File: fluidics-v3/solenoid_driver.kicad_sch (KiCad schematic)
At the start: 2 parts, among them J5 Screw_Terminal_01x06, U1 TPL7407LDR

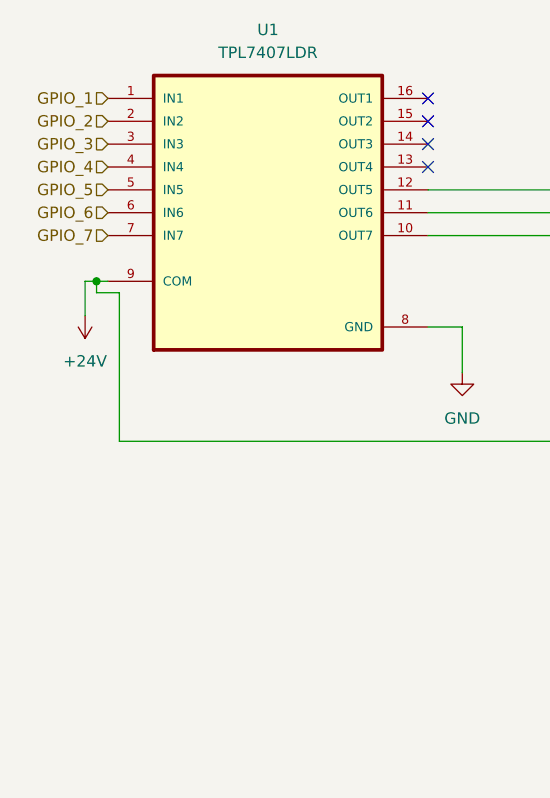
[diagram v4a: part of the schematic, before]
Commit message: v3: +24V soft-start front end, U1 COM bypass, silkscreen and BOM fixes
Power input stage
- Replace TH1 (10 ohm NTC) with a low-side N-channel soft-start: Q1 (F60N80,
  TO-220) with a 100k/68k gate divider (R2/R6) and 0.1u timing cap (C11).
  The NTC sat in series with the whole board and dissipated 1.5-10 W; at
  1.85 A it was already over a 7 mm disc's rating before any valve moved.
- Split ground: /GND1 (J1 shell + pin 2) is now separate from GND, with Q1
  bridging them. Removed a leftover 2.39 mm GND track that still touched
  J1.S2 and shorted straight across Q1.
- Add C12 470u/50V bulk and C13 0.1u HF bypass on +24V. C3 alone left the
  300 kHz - 100 MHz band uncovered while U4 switches at 500 kHz.
- Route the block: gate net kept inside 5 mm of Q1's gate; /GND1 return at
  1.50 mm (4.3 A capacity vs 1.85 A worst case through Q1).

Solenoid driver
- Add C25 0.1u across U1 pin 9 (COM) to GND. That node catches flyback from
  all seven channels and previously reached the +24V plane through ~50 mm of
  0.55 mm trace with nothing local.

Silkscreen
- Raise 403 graphic objects from 0.000/0.100/0.120/0.127 mm to the 0.15 mm
  fab minimum; five were zero-width, which is undefined behaviour. Fix one
  0.45 mm text height and one 0.09 mm stroke.
- Selector valve legend: label 'J23' named a part that does not exist; the
  connector there is J25. Recentre all 12 labels on their own connectors,
  strip stray newlines, and hide 7 duplicate footprint refdes that sat
  midway between connectors and read as shifted by one.

Cleanup
- Remove two /SDA and /SCL vias that connected B.Cu to B.Cu after those nets
  moved to the back layer, and split a +3.3V track so its end meets a
  junction rather than landing mid-span.
- Stitch an orphaned F.Cu ground island that had captured D3's cathode pad.

BOM
- Correct three MPNs that contradicted their own values and packages:
  R3 5.6k/0805 was a 680R 0603 part, R4 47k/0402 was a 4k7 0603 part,
  R5 3k/0402 was a 270R 0603 part.
- J1 car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
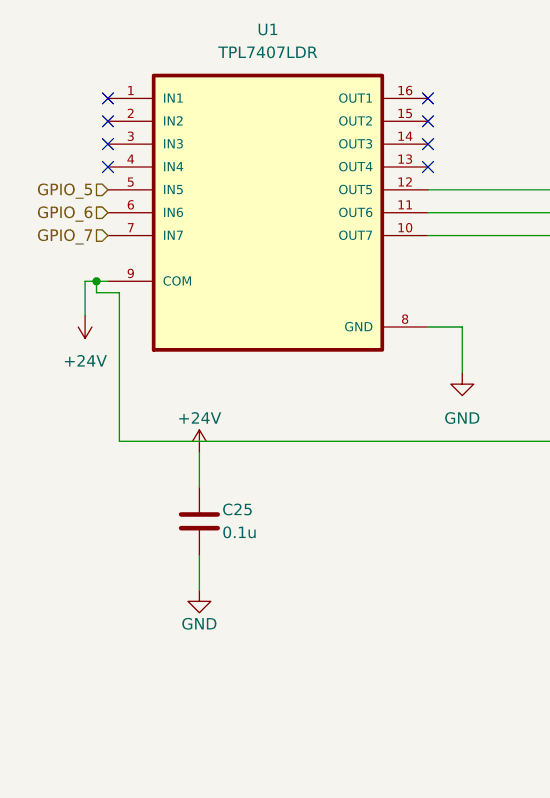
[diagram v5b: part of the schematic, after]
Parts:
- added C25: 0.1u, Capacitor_SMD:C_0603_1608Metric, symbol Device:C
- U1: MF Texas Instruments -> (none); MP TPL7407LDR -> (none); Manufacturer_Name (none) -> Texas Instruments; Manufacturer_Part_Number (none) -> TPL7407LDR
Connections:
- net +24V: now also C25.1
- net GND: now also C25.2
- net GPIO_1: no longer names the net of U1.1 (IN1)
- net GPIO_2: no longer names the net of U1.2 (IN2)
- net GPIO_3: no longer names the net of U1.3 (IN3)
- net GPIO_4: no longer names the net of U1.4 (IN4)
- no-connect marks 4 -> 8
